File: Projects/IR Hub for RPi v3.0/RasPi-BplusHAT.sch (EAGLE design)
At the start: 39 parts, among them SW1 SPST_TACT-KMR2, SW2 SPST_TACT-KMR2, SW3 SPST_TACT-KMR2, T1 2N4401, T2 2N4401, T3 2N4401, T4 2N4401

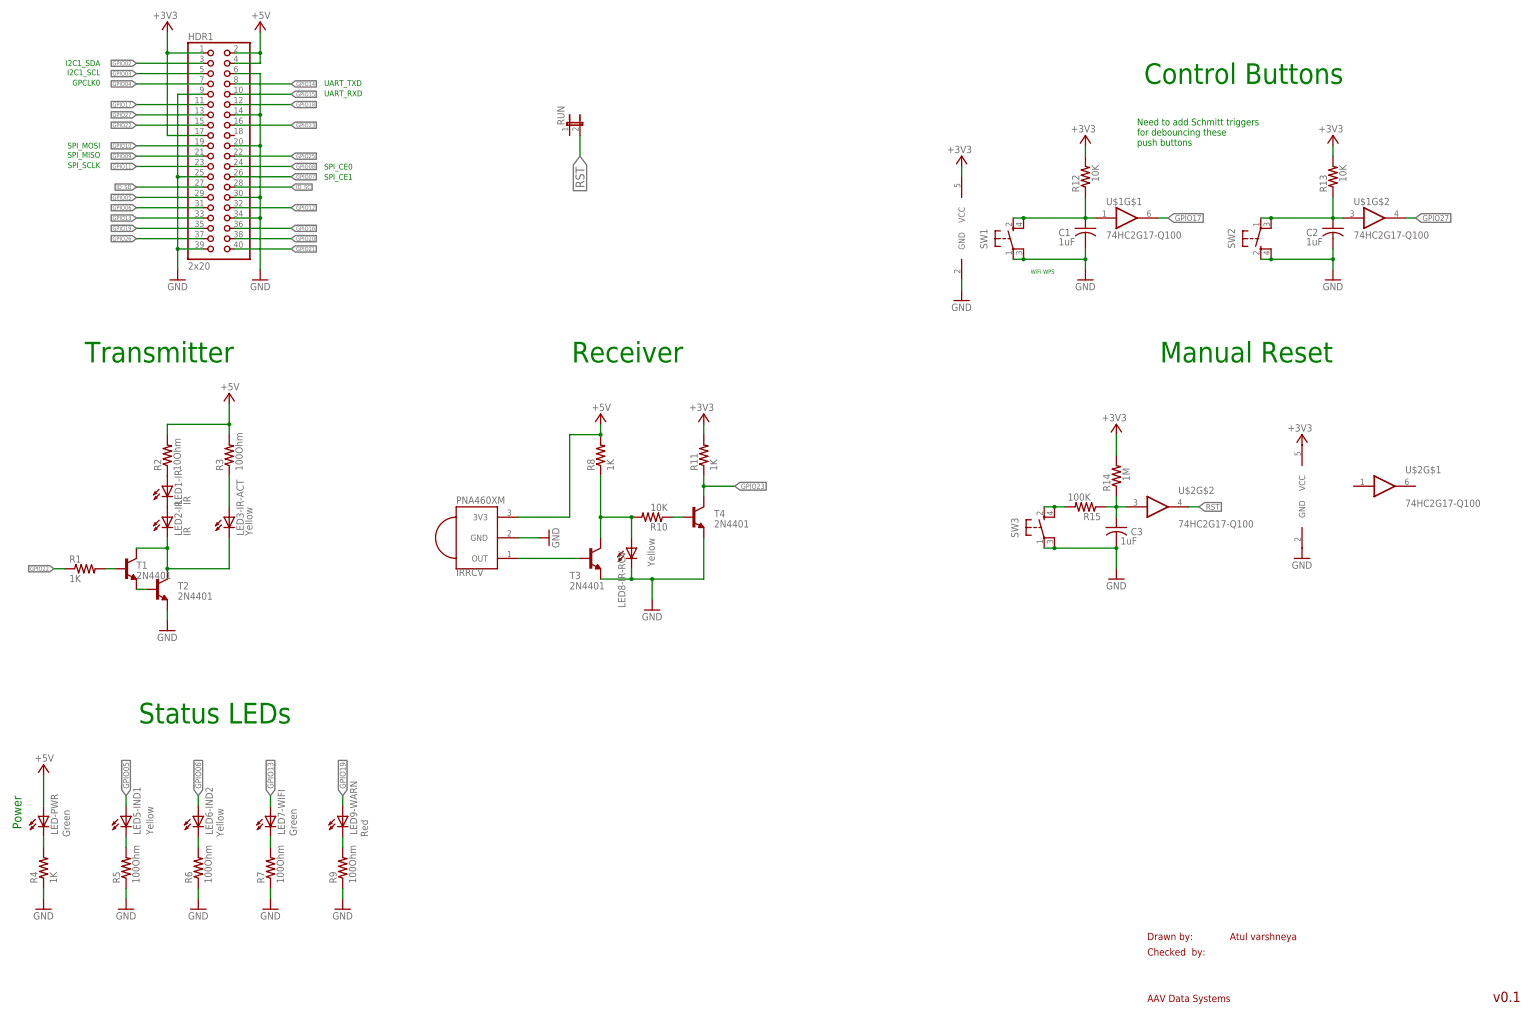
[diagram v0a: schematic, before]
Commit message: Revert "relocated IRRCV"
This reverts commit a5258da49ac38eba7fe15d274991cfdce8bd6922.
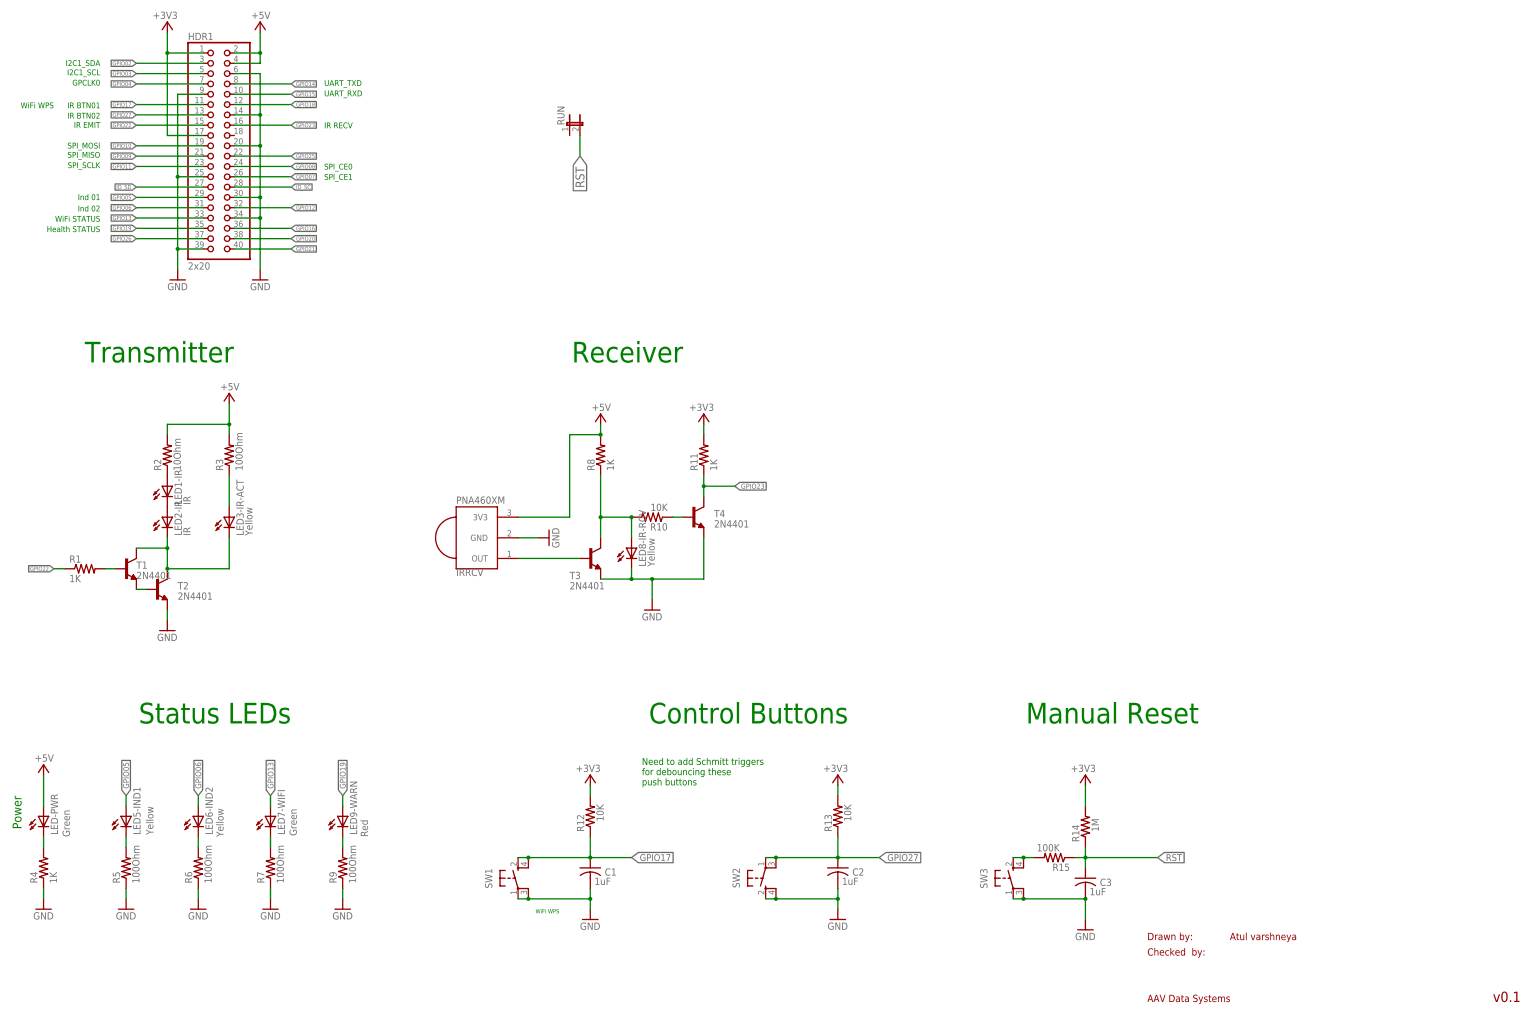
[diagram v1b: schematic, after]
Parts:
- removed U$1, U$2: 74HC2G17-Q100, varshneya:74HC2G17-Q100
- RUN: value RST -> (none)
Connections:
- removed net N$12: C2.1, R13.1, SW2.P, SW2.P1, U$1G$2.I
- removed net N$13: C3.1, R14.1, R15.1, U$2G$2.I
- removed net N$9: C1.1, R12.1, SW1.S, SW1.S1, U$1G$1.I
- net +3V3: no longer U$1G$3.VCC, U$2G$3.VCC
- net GND: no longer U$1G$3.GND, U$2G$3.GND
- net GPIO17: now also C1.1, R12.1, SW1.S, SW1.S1; no longer U$1G$1.O
- net GPIO27: now also C2.1, R13.1, SW2.P, SW2.P1; no longer U$1G$2.O
- net RST: now also C3.1, R14.1, R15.1; no longer U$2G$2.O
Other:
- moved on the sheet: C1, C2, C3, R12, R13, R14, R15, SW1, SW2, SW3
